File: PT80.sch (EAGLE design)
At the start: 78 parts, among them IC1 MAX1044, IC2 TL072P, IC3 78L05Z, IC4 78L12Z, Q1 2N5089

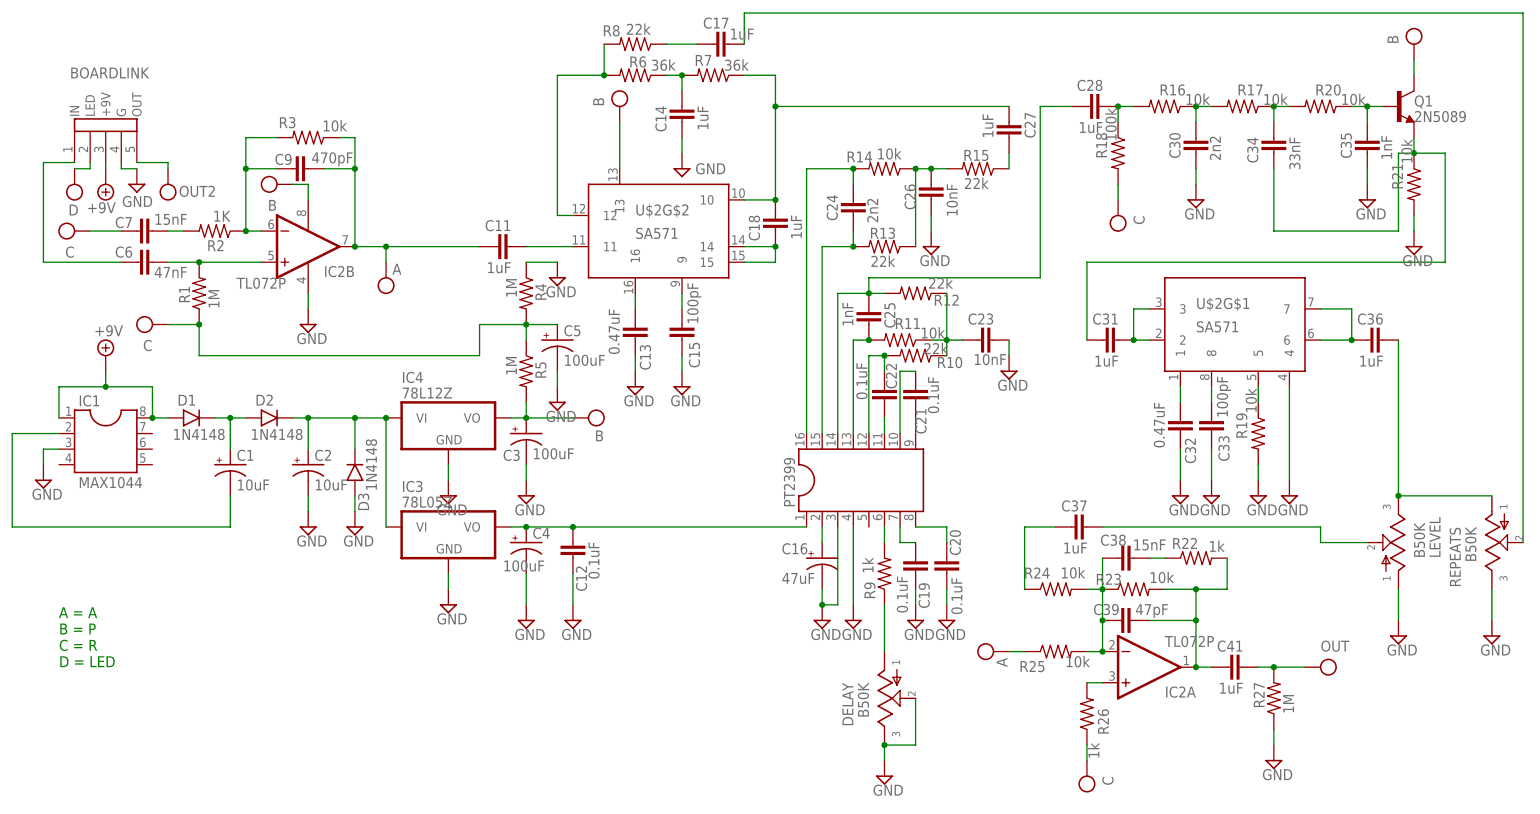
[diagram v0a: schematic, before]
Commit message: Version 1.1 - Fixed repeats direction and orientation of power regulators
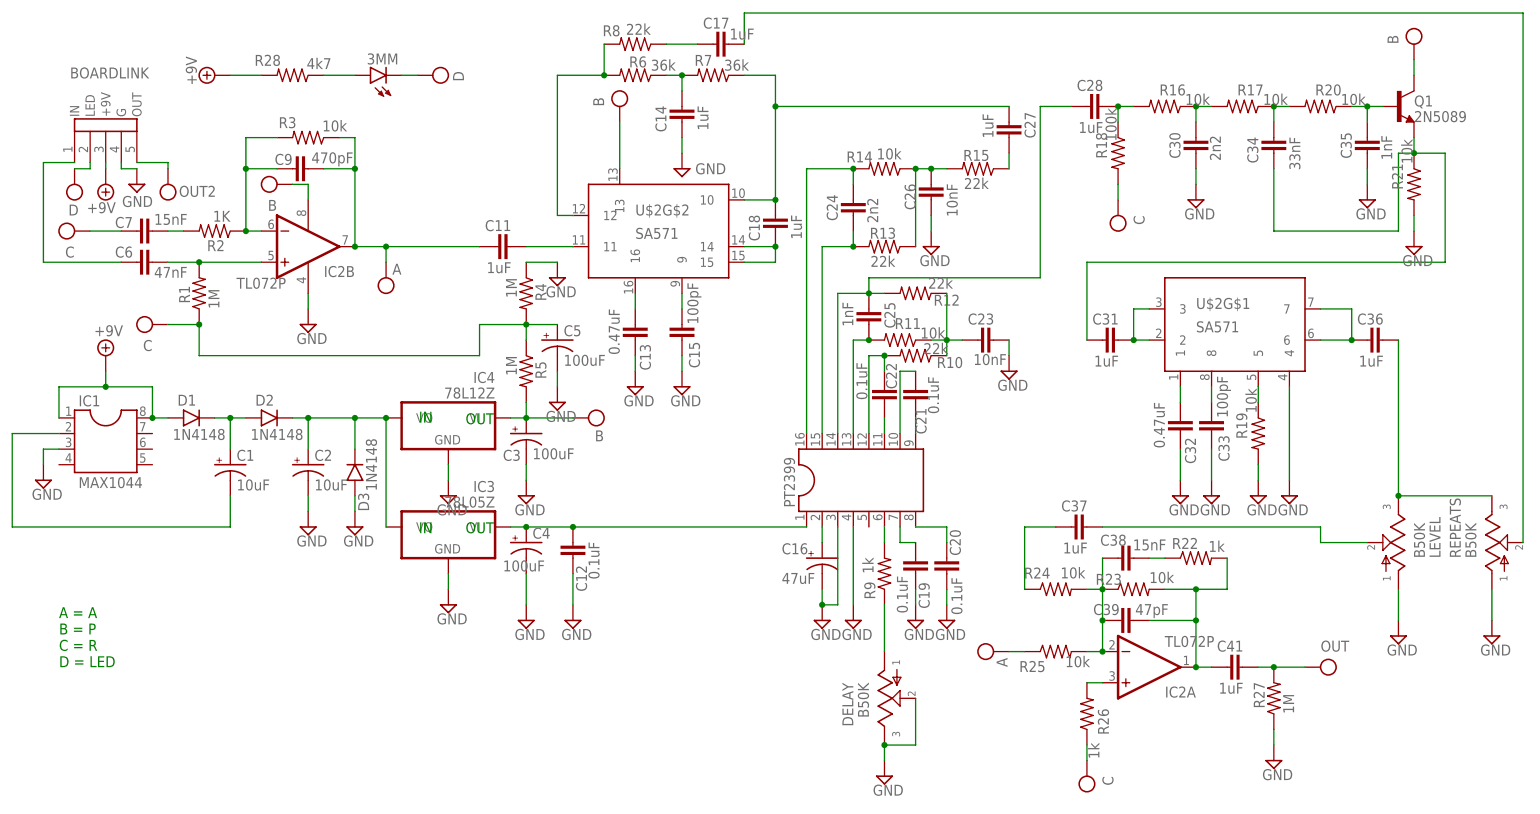
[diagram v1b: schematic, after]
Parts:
- added 3MM: LED3MM, mb_diodes:LED3MM
- added R28: 4k7, mb_resistors:6MM.3
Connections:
- new net N$1: C2.+, D2.C, D3.C, IC3.VO, IC4.VO
- net +9V: now also R28.2
- net B: now also IC4.VI; no longer IC4.VO
- net D: now also 3MM.C
- net GND: now also REPEATS.1; no longer REPEATS.3
- net N$4: now also 3MM.A, R28.1; no longer C2.+, D2.C, D3.C, IC3.VI, IC4.VI
- net N$48: now also REPEATS.3; no longer REPEATS.1
- net N$6: now also IC3.VI; no longer IC3.VO
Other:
- note added: "IN"
- note added: "OUT"
- moved on the sheet: REPEATS
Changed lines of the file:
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@@
 <part name="OUT" library="mb_supply" deviceset="OUT" device=""/>
 <part name="OUT2" library="mb_supply" deviceset="OUT" device=""/>
+<part name="R28" library="mb_resistors" deviceset="6MM" device=".3" value="4k7"/>
+<part name="V3" library="mb_supply" deviceset="+9V" device=""/>
+<part name="3MM" library="mb_diodes" deviceset="LED" device="3MM"/>
+<part name="D5" library="mb_supply" deviceset="D" device=""/>
 </parts>
 <sheets>
@@
 C = R
 D = LED</text>
+<text x="48.514" y="47.498" size="1.778" layer="91">IN</text>
+<text x="48.514" y="29.464" size="1.778" layer="91">IN</text>
+<text x="56.134" y="47.244" size="1.778" layer="91">OUT</text>
+<text x="56.134" y="29.464" size="1.778" layer="91">OUT</text>
 </plain>
 <instances>
@@
 <attribute name="VALUE" x="18.796" y="71.12" size="1.778" layer="96" rot="MR180"/>
 </instance>
-<instance part="IC3" gate="A1" x="53.34" y="30.48" smashed="yes">
-<attribute name="NAME" x="45.72" y="36.195" size="1.778" layer="95"/>
-<attribute name="VALUE" x="45.72" y="33.655" size="1.778" layer="96"/>
-</instance>
-<instance part="IC4" gate="A1" x="53.34" y="48.26" smashed="yes">
-<attribute name="NAME" x="45.72" y="53.975" size="1.778" layer="95"/>
-<attribute name="VALUE" x="45.72" y="51.435" size="1.778" layer="96"/>
+<instance part="IC3" gate="A1" x="53.34" y="30.48" smashed="yes" rot="MR0">
+<attribute name="NAME" x="60.96" y="36.195" size="1.778" layer="95" rot="MR0"/>
+<attribute name="VALUE" x="60.96" y="33.655" size="1.778" layer="96" rot="MR0"/>
+</instance>
+<instance part="IC4" gate="A1" x="53.34" y="48.26" smashed="yes" rot="MR0">
+<attribute name="NAME" x="60.96" y="53.975" size="1.778" layer="95" rot="MR0"/>
+<attribute name="VALUE" x="60.96" y="51.435" size="1.778" layer="96" rot="MR0"/>
 </instance>
 <instance part="C1" gate="1" x="17.78" y="40.64" smashed="yes">
@@
 <attribute name="VALUE" x="210.82" y="25.4" size="1.778" layer="96" rot="MR90"/>
 </instance>
-<instance part="REPEATS" gate="G$1" x="226.06" y="27.94" smashed="yes" rot="MR180">
-<attribute name="NAME" x="218.44" y="30.48" size="1.778" layer="95" rot="MR270"/>
-<attribute name="VALUE" x="220.98" y="30.48" size="1.778" layer="96" rot="MR270"/>
+<instance part="REPEATS" gate="G$1" x="226.06" y="27.94" smashed="yes">
+<attribute name="NAME" x="218.44" y="25.4" size="1.778" layer="95" rot="R90"/>
+<attribute name="VALUE" x="220.98" y="25.4" size="1.778" layer="96" rot="R90"/>
 </instance>
 <instance part="GND30" gate="GND" x="208.28" y="12.7" smashed="yes">
@@
 <instance part="OUT2" gate="G$1" x="7.62" y="86.36" smashed="yes" rot="R270">
 <attribute name="NAME" x="9.398" y="84.328" size="1.778" layer="95"/>
+</instance>
+<instance part="R28" gate="G$1" x="27.94" y="104.14" smashed="yes" rot="R180">
+<attribute name="NAME" x="26.035" y="107.4674" size="1.778" layer="95" rot="R180"/>
+<attribute name="VALUE" x="34.29" y="106.934" size="1.778" layer="96" rot="R180"/>
+</instance>
+<instance part="V3" gate="+9V" x="15.24" y="104.14" smashed="yes" rot="R90">
+<attribute name="VALUE" x="12.319" y="102.489" size="1.778" layer="96" rot="R90"/>
+</instance>
+<instance part="3MM" gate="G$1" x="43.18" y="104.14" smashed="yes" rot="R180">
+<attribute name="NAME" x="45.212" y="107.696" size="1.778" layer="95" rot="R180"/>
+</instance>
+<instance part="D5" gate="D" x="50.8" y="104.14" smashed="yes">
+<attribute name="VALUE" x="55.88" y="103.124" size="1.778" layer="96" rot="R90"/>
 </instance>
 </instances>
@@
 </segment>
 <segment>
-<pinref part="REPEATS" gate="G$1" pin="3"/>
-<pinref part="GND31" gate="GND" pin="GND"/>
-<wire x1="223.52" y1="20.32" x2="223.52" y2="15.24" width="0.1524" layer="91"/>
-</segment>
-<segment>
 <pinref part="U$1" gate="G$1" pin="G"/>
 <pinref part="GND32" gate="GND" pin="GND"/>
 <wire x1="0" y1="89.916" x2="0" y2="88.9" width="0.1524" layer="91"/>
 <wire x1="0" y1="88.9" x2="2.54" y2="88.9" width="0.1524" layer="91"/>
+</segment>
+<segment>
+<pinref part="REPEATS" gate="G$1" pin="1"/>
+<pinref part="GND31" gate="GND" pin="GND"/>
+<wire x1="223.52" y1="20.32" x2="223.52" y2="15.24" width="0.1524" layer="91"/>
 </segment>
 </net>
@@
 </segment>
 </net>
-<net name="N$4" class="0">
-<segment>
-<pinref part="C2" gate="1" pin="+"/>
-<pinref part="D2" gate="G$1" pin="C"/>
-<wire x1="30.48" y1="43.18" x2="30.48" y2="48.26" width="0.1524" layer="91"/>
-<wire x1="30.48" y1="48.26" x2="27.94" y2="48.26" width="0.1524" layer="91"/>
-<pinref part="D3" gate="G$1" pin="C"/>
-<wire x1="38.1" y1="43.18" x2="38.1" y2="48.26" width="0.1524" layer="91"/>
-<wire x1="38.1" y1="48.26" x2="30.48" y2="48.26" width="0.1524" layer="91"/>
-<junction x="30.48" y="48.26"/>
-<pinref part="IC4" gate="A1" pin="VI"/>
-<wire x1="43.18" y1="48.26" x2="38.1" y2="48.26" width="0.1524" layer="91"/>
-<junction x="38.1" y="48.26"/>
-<pinref part="IC3" gate="A1" pin="VI"/>
-<wire x1="43.18" y1="30.48" x2="43.18" y2="48.26" width="0.1524" layer="91"/>
-<junction x="43.18" y="48.26"/>
-</segment>
-</net>
 <net name="N$6" class="0">
 <segment>
-<pinref part="IC3" gate="A1" pin="VO"/>
 <pinref part="C4" gate="G$1" pin="+"/>
-<wire x1="63.5" y1="30.48" x2="66.04" y2="30.48" width="0.1524" layer="91"/>
 <pinref part="C12" gate="G$1" pin="2"/>
 <wire x1="73.66" y1="30.48" x2="66.04" y2="30.48" width="0.1524" layer="91"/>
-<junction x="66.04" y="30.48"/>
 <pinref part="PT2399" gate="G$1" pin="1"/>
 <wire x1="111.76" y1="30.48" x2="73.66" y2="30.48" width="0.1524" layer="91"/>
 <junction x="73.66" y="30.48"/>
+<pinref part="IC3" gate="A1" pin="VI"/>
+<wire x1="63.5" y1="30.48" x2="66.04" y2="30.48" width="0.1524" layer="91"/>
+<junction x="66.04" y="30.48"/>
 </segment>
 </net>
@@
 </segment>
 <segment>
-<pinref part="IC4" gate="A1" pin="VO"/>
 <pinref part="C3" gate="G$1" pin="+"/>
-<wire x1="63.5" y1="48.26" x2="66.04" y2="48.26" width="0.1524" layer="91"/>
 <pinref part="R5" gate="G$1" pin="2"/>
 <wire x1="66.04" y1="50.8" x2="66.04" y2="48.26" width="0.1524" layer="91"/>
@@
 <pinref part="B1" gate="B" pin="B"/>
 <wire x1="73.66" y1="48.26" x2="66.04" y2="48.26" width="0.1524" layer="91"/>
+<pinref part="IC4" gate="A1" pin="VI"/>
+<wire x1="63.5" y1="48.26" x2="66.04" y2="48.26" width="0.1524" layer="91"/>
 </segment>
 <segment>
@@
 <pinref part="LEVEL" gate="G$1" pin="3"/>
 <wire x1="208.28" y1="60.96" x2="208.28" y2="35.56" width="0.1524" layer="91"/>
-<pinref part="REPEATS" gate="G$1" pin="1"/>
+<pinref part="REPEATS" gate="G$1" pin="3"/>
 <wire x1="223.52" y1="35.56" x2="208.28" y2="35.56" width="0.1524" layer="91"/>
 <junction x="208.28" y="35.56"/>
@@
 <wire x1="-5.08" y1="89.916" x2="-5.08" y2="88.9" width="0.1524" layer="91"/>
 <wire x1="-5.08" y1="88.9" x2="-7.62" y2="88.9" width="0.1524" layer="91"/>
+</segment>
+<segment>
+<pinref part="D5" gate="D" pin="D"/>
+<pinref part="3MM" gate="G$1" pin="C"/>
+<wire x1="48.26" y1="104.14" x2="45.72" y2="104.14" width="0.1524" layer="91"/>
 </segment>
 </net>
@@
 <junction x="-2.54" y="53.34"/>
 </segment>
+<segment>
+<pinref part="V3" gate="+9V" pin="+9V"/>
+<pinref part="R28" gate="G$1" pin="2"/>
+<wire x1="17.78" y1="104.14" x2="22.86" y2="104.14" width="0.1524" layer="91"/>
+</segment>
 </net>
 <net name="OUT" class="0">
@@
 </segment>
 </net>
+<net name="N$1" class="0">
+<segment>
+<pinref part="IC3" gate="A1" pin="VO"/>
+<pinref part="IC4" gate="A1" pin="VO"/>
+<wire x1="43.18" y1="30.48" x2="43.18" y2="48.26" width="0.1524" layer="91"/>
+<pinref part="C2" gate="1" pin="+"/>
+<pinref part="D2" gate="G$1" pin="C"/>
+<wire x1="30.48" y1="43.18" x2="30.48" y2="48.26" width="0.1524" layer="91"/>
+<wire x1="30.48" y1="48.26" x2="27.94" y2="48.26" width="0.1524" layer="91"/>
+<pinref part="D3" gate="G$1" pin="C"/>
+<wire x1="38.1" y1="43.18" x2="38.1" y2="48.26" width="0.1524" layer="91"/>
+<wire x1="38.1" y1="48.26" x2="30.48" y2="48.26" width="0.1524" layer="91"/>
+<junction x="30.48" y="48.26"/>
+<wire x1="43.18" y1="48.26" x2="38.1" y2="48.26" width="0.1524" layer="91"/>
+<junction x="43.18" y="48.26"/>
+<junction x="38.1" y="48.26"/>
+</segment>
+</net>
+<net name="N$4" class="0">
+<segment>
+<pinref part="3MM" gate="G$1" pin="A"/>
+<pinref part="R28" gate="G$1" pin="1"/>
+<wire x1="38.1" y1="104.14" x2="33.02" y2="104.14" width="0.1524" layer="91"/>
+</segment>
+</net>
